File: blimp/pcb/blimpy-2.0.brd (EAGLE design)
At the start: 80 x 70 mm, 153 parts, among them J1 MICRO-USB, J10 3-PIN SMD, J11 3-PIN SMD, J12 3-PIN SMD, J13 3-PIN SMD, J14 3-PIN SMD, J9 3-PIN SMD, M0 DRV8833PWPR, M1 DRV8833PWPR, M2 DRV8833PWPR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

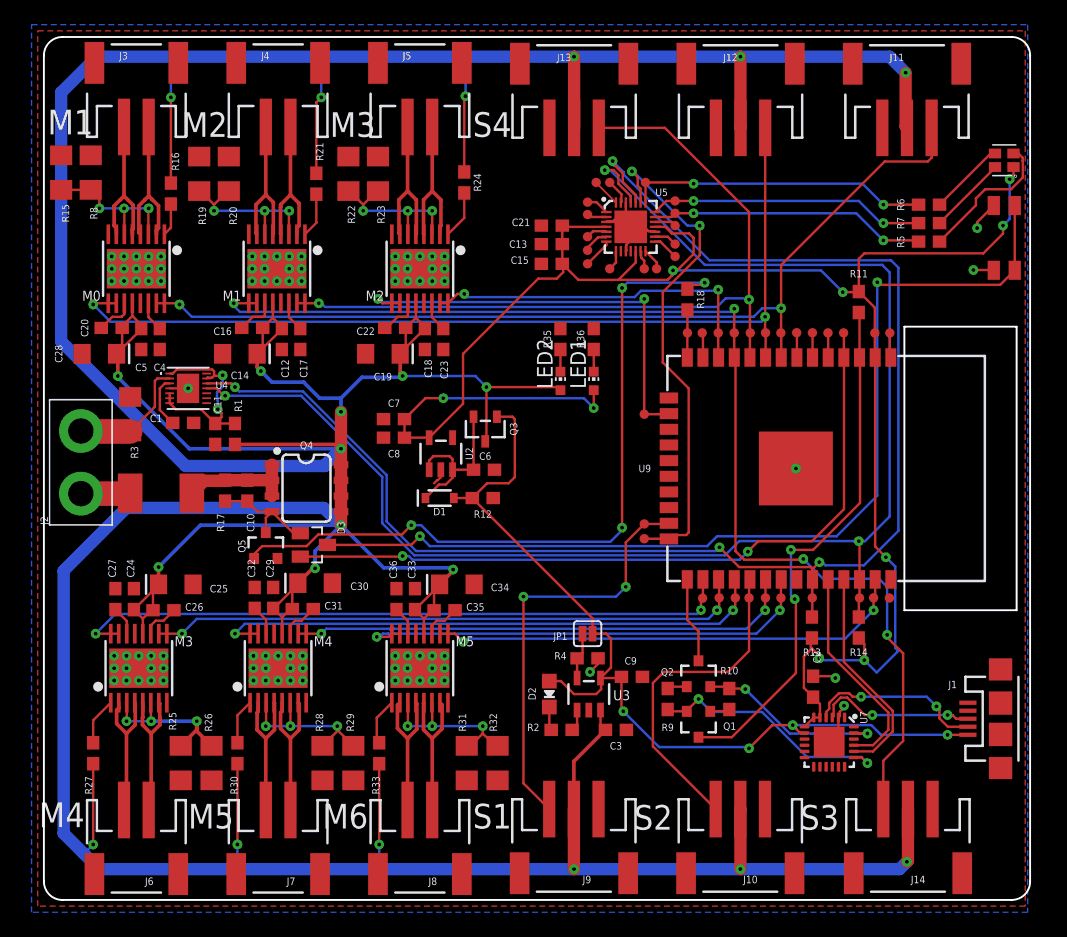
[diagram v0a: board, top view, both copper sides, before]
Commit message: Added LED connector
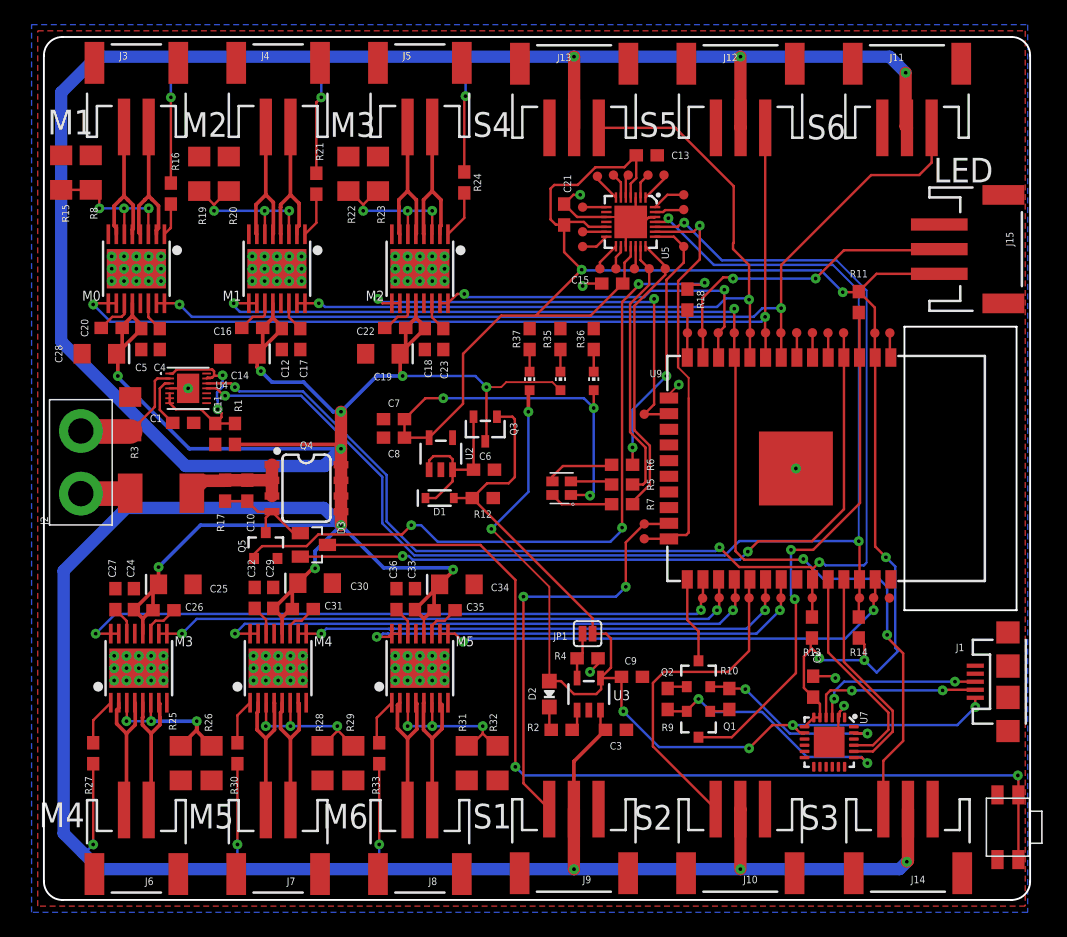
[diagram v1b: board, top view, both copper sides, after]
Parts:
- added J15: 3-PIN SMD, SparkFun-Connectors:JST-3-SMD
- added LED3: VUSB, led:CHIP-LED0603
- added R37: (no value), SparkFun-Resistors:0603
- LED1: value (none) -> 3.3V
- LED2: value (none) -> VBAT
- moved U$1 47.8 mm to (78.2, 5.90)
- moved U1 44.7 mm to (42.0, 33.4)
- moved R7 33.8 mm to (46.9, 32.1), turned to 0 degrees
- moved R6 32.6 mm to (46.9, 35.3), turned to 0 degrees
- moved R5 31.8 mm to (46.9, 33.7), turned to 0 degrees
- moved C13 10.5 mm to (48.9, 60.4), turned to 0 degrees
- moved TP28 7.17 mm to (51.9, 57.2)
- moved TP33 7.14 mm to (44.9, 58.7)
- moved TP29 6.58 mm to (50.3, 58.8)
- moved TP32 6.45 mm to (46.2, 58.8)
- moved TP27 6.39 mm to (51.9, 56.0)
- moved TP36 6.26 mm to (43.7, 53.0)
- moved TP37 6.18 mm to (45.1, 51.2)
- moved TP42 6.05 mm to (51.9, 53.0)
- moved TP31 5.99 mm to (47.4, 58.8)
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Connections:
- removed net LEDRING: TP5.P$1, U9.13
- new net LEDEXT: J15.2, TP5.P$1, U9.13
- new net N$17: LED3.C, R37.1
- net 3.3V: now also J15.3
- net GND: now also J15.1, R37.2
- net V_USB: now also LED3.A
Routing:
- net V_USB: track 74.1 -> 102.5 mm, vias 4 -> 6
- net LEDEXT: track 0.00 -> 27.3 mm, vias 0 -> 2
- net SDA: track 122.7 -> 108.3 mm
- net SCL: track 121.0 -> 107.0 mm
- net 3.3V: track 154.5 -> 166.0 mm, vias 9 -> 8
- net N$9: track 11.7 -> 3.40 mm
- net IO1-RST: track 41.0 -> 33.6 mm, vias 2 -> 1
- net GREEN: track 24.5 -> 22.1 mm
- net LEDRING: track 2.02 -> 0.00 mm
- net N$17: track 0.00 -> 1.80 mm
- net N$22: track 81.2 -> 79.5 mm
- net GND: track 26.1 -> 27.4 mm, vias 92 -> 98
- net N$10: track 6.41 -> 5.11 mm
- net BLUE: track 22.6 -> 23.7 mm, vias 2 -> 0
- net PWM2-B: track 35.3 -> 36.4 mm
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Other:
- board text added: "Blimpy Board 2.0 Immersive Arts Space"
- board text added: "LED"
- board text added: "S5"
- board text added: "S6"
- board text removed: "Blimpy Board 2.0 Immersive Arts Space ZHdK - Joël Gähwiler"

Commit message: Cosmetic changes
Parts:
- Q1, Q2: value mmbt2222 -> 600mA/40V; device SparkFun:SOT23-3 -> SparkFun-DiscreteSemi:SOT23-3
- R3: value 0.05 -> 0.005
- moved R16 0.82 mm to (10.5, 58.1)
- moved R19 0.50 mm to (13.1, 58.9)
- moved R20 0.50 mm to (15.5, 58.9)
- moved R15 0.30 mm to (1.70, 59.0)
- moved R8 0.30 mm to (4.10, 59.0)
- moved R21 0.20 mm to (22.3, 58.1)
- moved Q1 0.10 mm to (53.2, 14.3)
- moved Q2 0.10 mm to (53.2, 18.3)
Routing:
- net V_USB: track 102.5 -> 100.1 mm
- net N$14: track 12.4 -> 13.5 mm
- net N$5: track 2.68 -> 3.55 mm
- net V_BATT: track 491.1 -> 490.3 mm
- net N$28: track 13.7 -> 13.2 mm
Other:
- board text added: "+"
- board text added: "-"
- board text added: "0"
- board text added: "1"
- board text added: "10"
- board text added: "11"
- board text added: "12"
- board text added: "2"
- board text added: "3"
- board text added: "4"
- board text added: "5"
- board text added: "6"
- board text added: "7"
- board text added: "8"
- board text added: "9"
- board text added: "Maximum Ratings 1S Battery (3.7V nom.) / 10 A"
- board text removed: "Maximum Ratings Battery 3A (cum.) Actors 2A (indv.)"

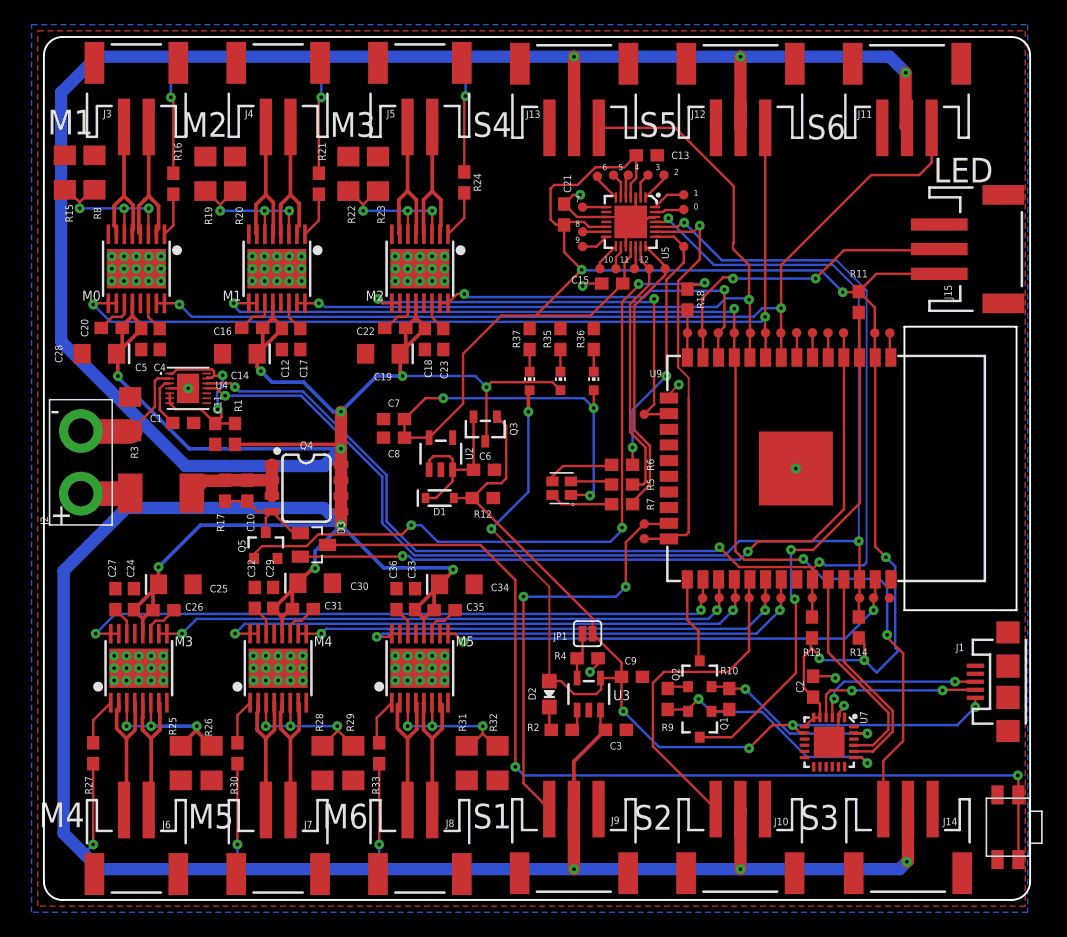
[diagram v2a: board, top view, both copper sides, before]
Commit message: Motor driver bug fix, added pull-up for btn input, cosmetic changes
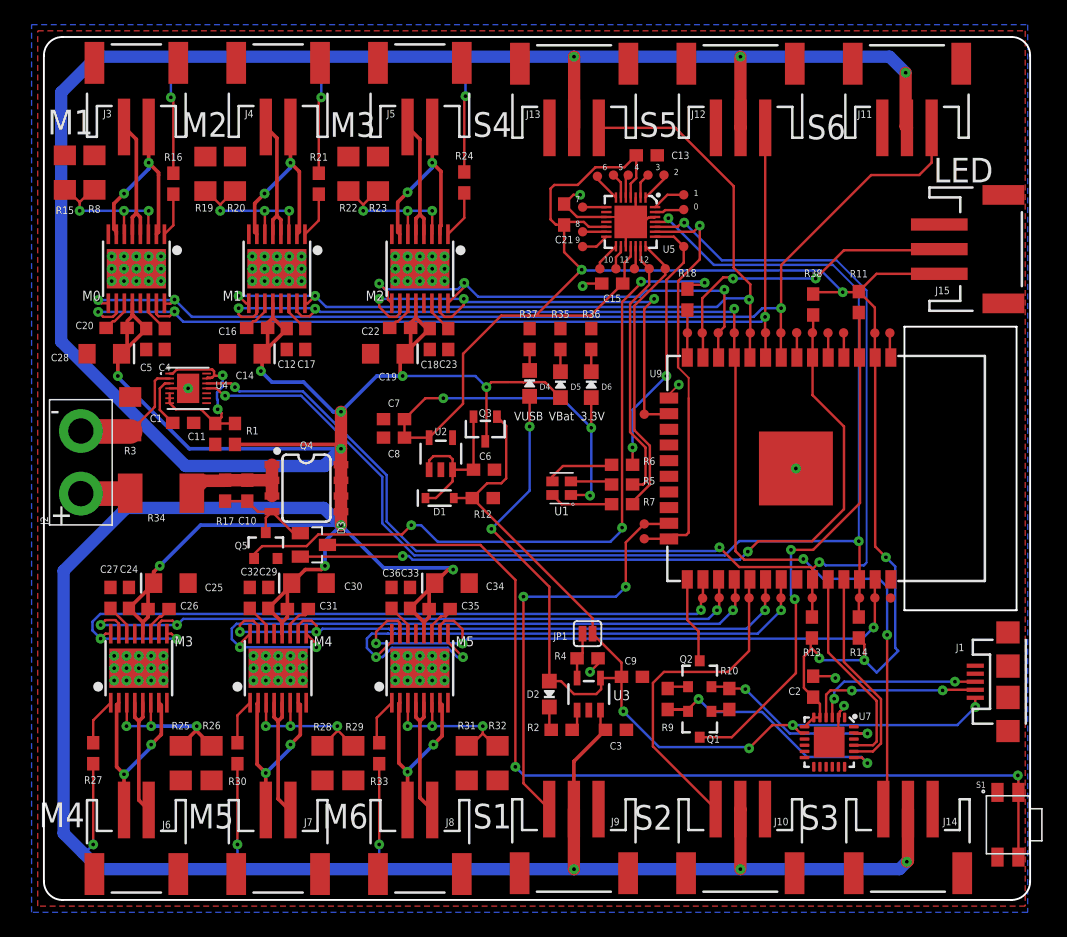
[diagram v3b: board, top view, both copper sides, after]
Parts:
- removed LED1: 3.3V, led:CHIP-LED0603
- removed LED2: VBAT, led:CHIP-LED0603
- removed LED3: VUSB, led:CHIP-LED0603
- removed U$1: EVQPUJ02K, chlimax:EVQPUJ02K
- added D4, D5, D6: GREEN, microbuilder:CHIPLED_0805_NOOUTLINE
- added R38: 4.7k, SparkFun-Resistors:0603
- added S1: EVQPUJ02K, chlimax:EVQPUJ02K
- moved C30 0.50 mm to (21.5, 25.7)
- moved C33 0.41 mm to (29.7, 24.5)
- moved C36 0.41 mm to (28.2, 24.5)
- moved C24 0.41 mm to (6.90, 24.5)
- moved C27 0.41 mm to (5.40, 24.5)
- moved C26 0.41 mm to (9.30, 23.6)
- moved C35 0.41 mm to (32.1, 23.6)
- moved C25 0.41 mm to (10.3, 25.7)
- moved C34 0.41 mm to (33.1, 25.7)
- moved C16 0.40 mm to (17.3, 46.4)
- moved C18 0.40 mm to (31.3, 45.5)
- moved C29 0.40 mm to (18.2, 24.5)
- moved C32 0.40 mm to (16.7, 24.5)
- moved C14 0.40 mm to (16.3, 44.3)
- moved C20 0.40 mm to (5.90, 46.4)
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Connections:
- removed net N$20: TP8.P$1, U9.6
- removed net PWM0-A: J11.3, M0.15, M0.16, TP1.P$1, U9.8
- removed net PWM0-B: J12.3, M0.10, M0.9, TP2.P$1, U9.9
- removed net PWM1-A: J13.3, M1.15, M1.16, TP3.P$1, U9.10
- removed net PWM1-B: J14.3, M1.10, M1.9, TP6.P$1, U9.11
- removed net PWM2-A: M2.15, M2.16, TP17.P$1, U9.12
- removed net PWM2-B: M2.10, M2.9, TP23.P$1, U9.16
- removed net PWM3-A: M3.15, M3.16, TP16.P$1, U9.26
- removed net PWM3-B: M3.10, M3.9, TP15.P$1, U9.27
- removed net PWM4-A: M4.15, M4.16, TP22.P$1, U9.28
- removed net PWM4-B: M4.10, M4.9, TP21.P$1, U9.30
- removed net PWM5-A: M5.15, M5.16, TP20.P$1, U9.31
- removed net PWM5-B: M5.10, M5.9, TP14.P$1, U9.37
- new net N$58: J3.1, M0.4, M0.5
- new net PWM0-1: J11.3, M0.16, M0.9, TP1.P$1, U9.8
- new net PWM0-2: J12.3, M0.10, M0.15, TP2.P$1, U9.9
- new net PWM1-1: J13.3, M1.16, M1.9, TP3.P$1, U9.10
- new net PWM1-2: J14.3, M1.10, M1.15, TP6.P$1, U9.11
- new net PWM2-1: M2.16, M2.9, TP17.P$1, U9.12
- new net PWM2-2: M2.10, M2.15, TP23.P$1, U9.16
- new net PWM3-1: M3.16, M3.9, TP16.P$1, U9.26
- new net PWM3-2: M3.10, M3.15, TP15.P$1, U9.27
- new net PWM4-1: M4.16, M4.9, TP22.P$1, U9.28
- new net PWM4-2: M4.10, M4.15, TP21.P$1, U9.30
- new net PWM5-1: M5.16, M5.9, TP20.P$1, U9.31
- new net PWM5-2: M5.10, M5.15, TP14.P$1, U9.37
- net 3.3V: now also D6.A, R38.2; no longer LED1.A
- net BTN: now also R38.1, TP8.P$1, U9.6; no longer TP10.P$1, U9.4
- net GND: now also S1.1, S1.3; no longer U$1.1, U$1.3
- net N$17: now also D4.C; no longer LED3.C
- net N$22: now also S1.2, S1.4; no longer U$1.2, U$1.4
- net N$24: now also J4.1, M1.5; no longer J4.2, M1.2
- net N$25: now also J4.2, M1.2; no longer J4.1, M1.5
- net N$30: now also J6.1, M3.4, M3.5; no longer J5.2, M2.2, M2.4
- net N$31: now also M2.4; no longer M2.7
- net N$36: now also M3.7; no longer M3.4
- net N$37: now also M0.7; no longer M0.4
- net N$38: now also J7.1, M4.4, M4.5; no longer J6.1, M3.5, M3.7
- net N$43: now also J8.2, M5.2, M5.7; no longer J7.2, M4.2, M4.4
- net N$44: now also J7.2, M4.2; no longer J7.1, M4.5
- net N$48: now also J5.2, M2.2, M2.7; no longer J3.1, M0.5, M0.7
- net N$50: now also J8.1, M5.5; no longer J8.2, M5.2
- net N$51: now also D6.C, R36.1; no longer J8.1, M5.5, M5.7
- net N$56: now also D5.C; no longer LED2.C
- net N$57: now also TP10.P$1, U9.4; no longer LED1.C, R36.1
- net V_BATT: now also D5.A; no longer LED2.A
- net V_USB: now also D4.A; no longer LED3.A
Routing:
- net PWM1-2: track 0.00 -> 97.5 mm, vias 0 -> 5
- net PWM1-B: track 95.5 -> 0.00 mm, vias 4 -> 0
- net PWM0-1: track 0.00 -> 84.3 mm, vias 0 -> 3
- net PWM0-2: track 0.00 -> 78.6 mm, vias 0 -> 3
- net PWM0-A: track 77.4 -> 0.00 mm, vias 2 -> 0
- net PWM0-B: track 75.9 -> 0.00 mm, vias 2 -> 0
- net PWM1-1: track 0.00 -> 71.8 mm, vias 0 -> 3
- net PWM1-A: track 64.6 -> 0.00 mm, vias 2 -> 0
- net PWM3-1: track 0.00 -> 62.1 mm, vias 0 -> 3
- net PWM3-2: track 0.00 -> 58.2 mm, vias 0 -> 3
- net PWM4-1: track 0.00 -> 54.8 mm, vias 0 -> 3
- net PWM3-A: track 54.3 -> 0.00 mm, vias 2 -> 0
- net PWM5-2: track 0.00 -> 53.1 mm, vias 0 -> 3
- net PWM4-2: track 0.00 -> 51.9 mm, vias 0 -> 3
- net PWM5-1: track 0.00 -> 51.4 mm, vias 0 -> 3
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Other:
- board text added: "3.3V"
- board text added: "Blimpy Board 2.0 Immersive Arts Space, ZHdK"
- board text added: "R34"
- board text added: "U1"
- board text added: "VBat"
- board text added: "VUSB"
- board text removed: "Blimpy Board 2.0 Immersive Arts Space"
